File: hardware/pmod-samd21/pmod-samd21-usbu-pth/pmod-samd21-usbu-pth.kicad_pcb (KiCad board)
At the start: 2 copper layers, 18.2 x 31.1 mm, 19 parts, among them J1 PMOD-2x6-MALE, J2 PMOD-2x6-FEMALE, J3 USB_B_Micro, J4 CORTEX_DEBUGPTH, Q1 2N7002PW, U1 ATSAMD21G-A, Y1 32.768kHz

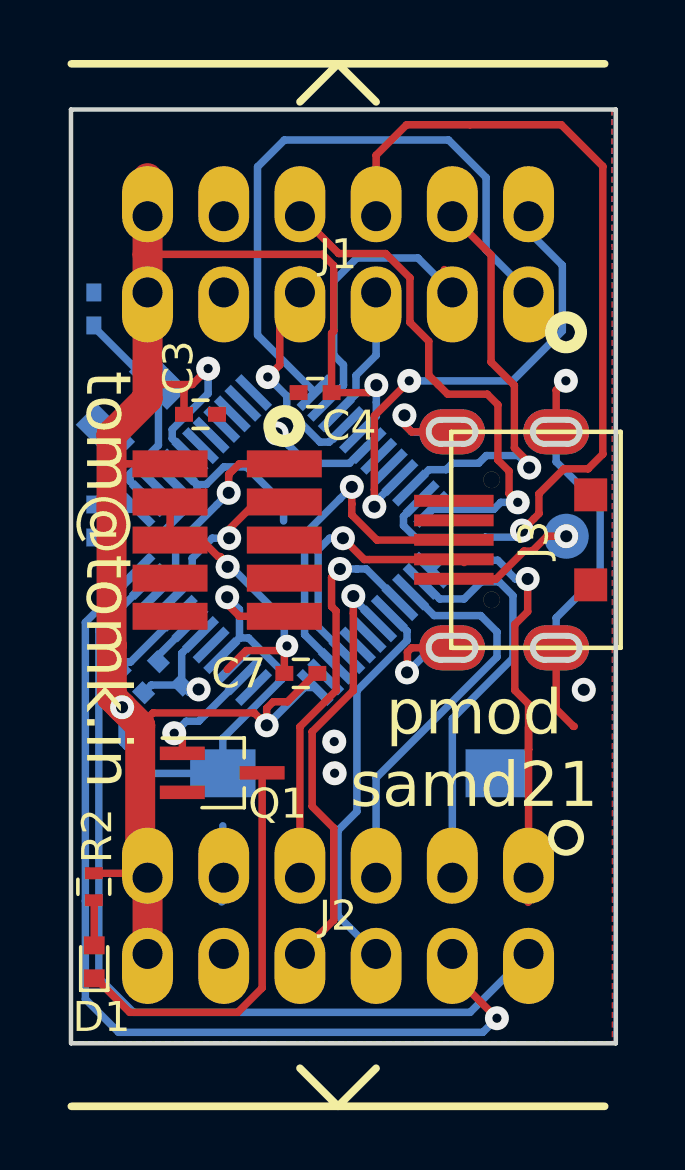
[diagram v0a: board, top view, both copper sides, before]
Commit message: pmod-samd21: routed pth version with spi/i2c compatibile addressing
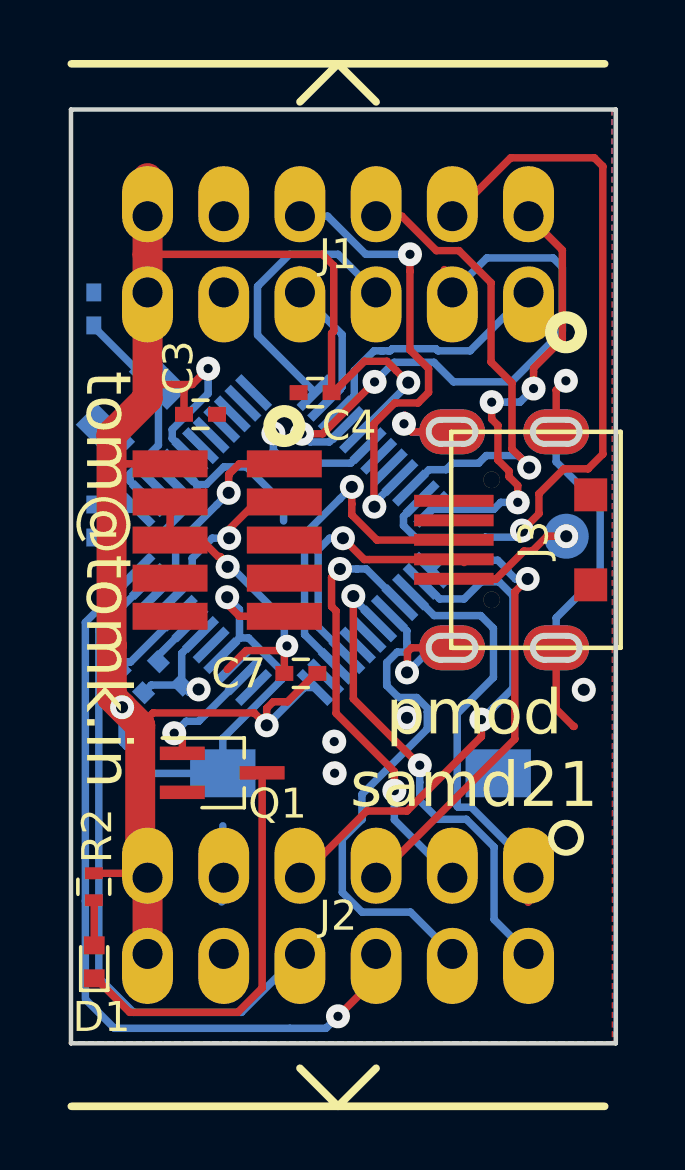
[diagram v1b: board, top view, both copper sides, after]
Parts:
- C5, C6: value 15pF -> 6pF
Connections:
- J1 pad 1: /SER0_0 -> /PA10+SER0_2+SS
- J1 pad 10: /SER2_3 -> /PA12+SER2_0+SDA
- J1 pad 2: /SER0_1 -> /PA11+SER0_3+MOSI
- J1 pad 3: /SER0_2 -> /PA08+SER0_0+MISO
- J1 pad 4: /SER0_3 -> /PA09+SER0_1+SCK
- J1 pad 7: /SER2_0 -> /PA15+SER2_3
- J1 pad 8: /SER2_1 -> /PA14+SER2_2
- J1 pad 9: /SER2_2 -> /PA13+SER2_1+SCL
- J2 pad 1: /SER1_0 -> /PA18+SER1_2+SS
- J2 pad 10: /SER5_3 -> /PB02+SER5_0+SDA
- J2 pad 2: /SER1_1 -> /PA19+SER1_3+MOSI
- J2 pad 3: /SER1_2 -> /PA16+SER1_0+MISO
- J2 pad 4: /SER1_3 -> /PA17+SER1_1+SCK
- J2 pad 7: /SER5_0 -> /PA21+SER5_3
- J2 pad 8: /SER5_1 -> /PA20+SER5_2
- J2 pad 9: /SER5_2 -> /PB03+SER5_1+SCL
- J3 pad 4: (no net) -> Net-(J3-Pad4)
- J4 pad 6: (no net) -> Net-(J4-Pad6)
- J4 pad 7: (no net) -> Net-(J4-Pad7)
- J4 pad 8: (no net) -> Net-(J4-Pad8)
- J4 pad 9: (no net) -> Net-(J4-Pad9)
- U1 pad 10: (no net) -> Net-(U1-Pad10)
- U1 pad 11: (no net) -> Net-(U1-Pad11)
- U1 pad 12: (no net) -> Net-(U1-Pad12)
- U1 pad 13: /SER0_0 -> /PA08+SER0_0+MISO
- U1 pad 14: /SER0_1 -> /PA09+SER0_1+SCK
- U1 pad 15: /SER0_2 -> /PA10+SER0_2+SS
- U1 pad 16: /SER0_3 -> /PA11+SER0_3+MOSI
- U1 pad 19: (no net) -> Net-(U1-Pad19)
- U1 pad 20: (no net) -> Net-(U1-Pad20)
- U1 pad 21: /SER2_0 -> /PA12+SER2_0+SDA
- U1 pad 22: /SER2_1 -> /PA13+SER2_1+SCL
- U1 pad 23: /SER2_2 -> /PA14+SER2_2
- U1 pad 24: /SER2_3 -> /PA15+SER2_3
- U1 pad 25: /SER1_0 -> /PA16+SER1_0+MISO
- U1 pad 26: /SER1_1 -> /PA17+SER1_1+SCK
- U1 pad 27: /SER1_2 -> /PA18+SER1_2+SS
- U1 pad 28: /SER1_3 -> /PA19+SER1_3+MOSI
- U1 pad 29: /SER5_2 -> /PA20+SER5_2
- U1 pad 3: (no net) -> Net-(U1-Pad3)
- U1 pad 30: /SER5_3 -> /PA21+SER5_3
- U1 pad 31: (no net) -> Net-(U1-Pad31)
- U1 pad 32: (no net) -> Net-(U1-Pad32)
- U1 pad 37: (no net) -> Net-(U1-Pad37)
- U1 pad 39: (no net) -> Net-(U1-Pad39)
- U1 pad 4: (no net) -> Net-(U1-Pad4)
- U1 pad 41: (no net) -> Net-(U1-Pad41)
- U1 pad 47: /SER5_0 -> /PB02+SER5_0+SDA
- U1 pad 48: /SER5_1 -> /PB03+SER5_1+SCL
- U1 pad 7: (no net) -> Net-(U1-Pad7)
- U1 pad 8: (no net) -> Net-(U1-Pad8)
- U1 pad 9: (no net) -> Net-(U1-Pad9)
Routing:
- net /SER5_1: track 32.1 -> 0.00 mm, vias 1 -> 0
- net /SER5_0: track 30.1 -> 0.00 mm
- net /SER2_2: track 28.5 -> 0.00 mm, vias 1 -> 0
- net /PB03+SER5_1+SCL: track 0.00 -> 26.6 mm, vias 0 -> 1
- net /PA14+SER2_2: track 0.00 -> 25.9 mm, vias 0 -> 1
- net /SER0_0: track 22.9 -> 0.00 mm
- net /PB02+SER5_0+SDA: track 0.00 -> 21.9 mm
- net /PA11+SER0_3+MOSI: track 0.00 -> 19.3 mm, vias 0 -> 2
- net /SER2_0: track 17.9 -> 0.00 mm, vias 2 -> 0
- net /PA20+SER5_2: track 0.00 -> 17.5 mm
- net /SER2_3: track 17.2 -> 0.00 mm, vias 1 -> 0
- net /PA15+SER2_3: track 0.00 -> 17.2 mm, vias 0 -> 3
- net /PA17+SER1_1+SCK: track 0.00 -> 16.9 mm, vias 0 -> 1
- net /PA21+SER5_3: track 0.00 -> 16.7 mm, vias 0 -> 2
- net /PA13+SER2_1+SCL: track 0.00 -> 16.1 mm, vias 0 -> 1
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
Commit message: pmod-samd21: Fix PCB rev in silk
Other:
- board text added: "Sep 2019"
- board text removed: "Jan 2019"
